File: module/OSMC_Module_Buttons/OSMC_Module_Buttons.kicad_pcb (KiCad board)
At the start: 4 copper layers, 34 x 41 mm, 4 parts, among them J1 Conn_01x08_Socket, U1 OSMC Module Board w/pins, U2 24LC02BT-I/OT, U3 PCF8574DWR

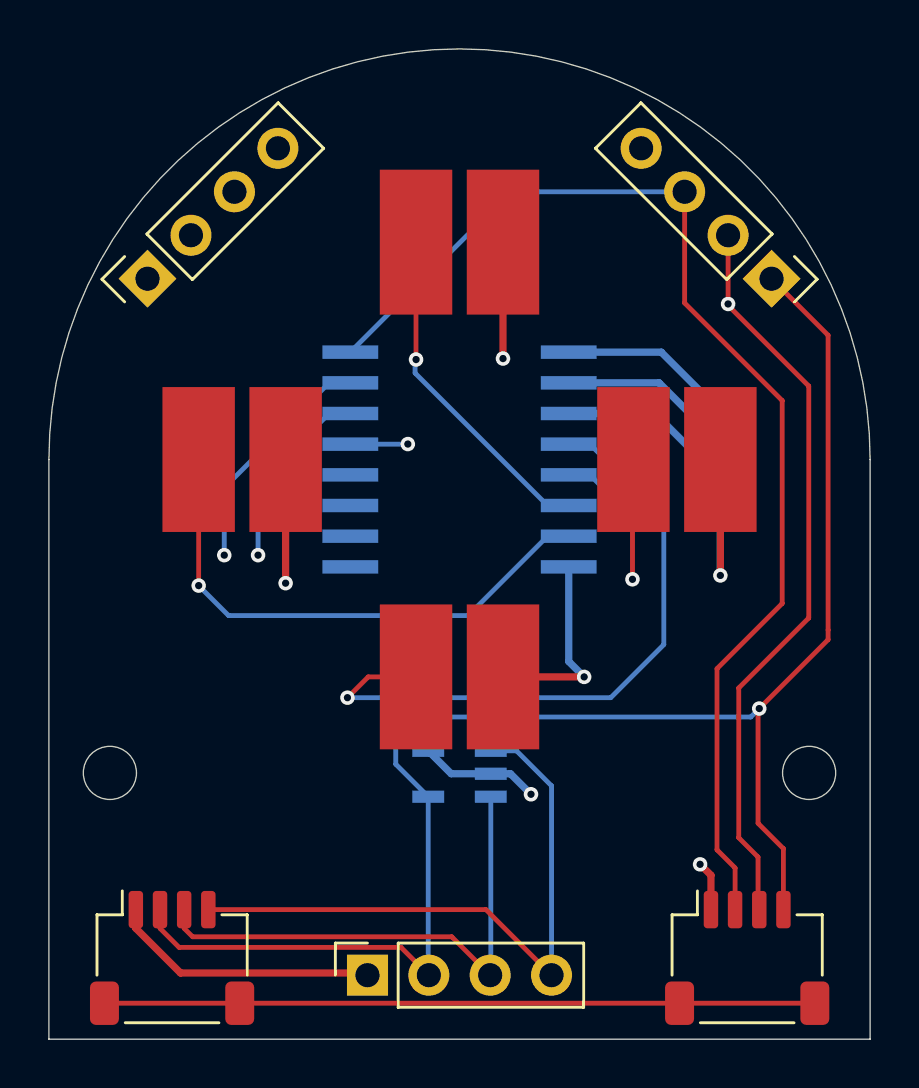
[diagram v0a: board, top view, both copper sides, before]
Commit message: cleared via and traces
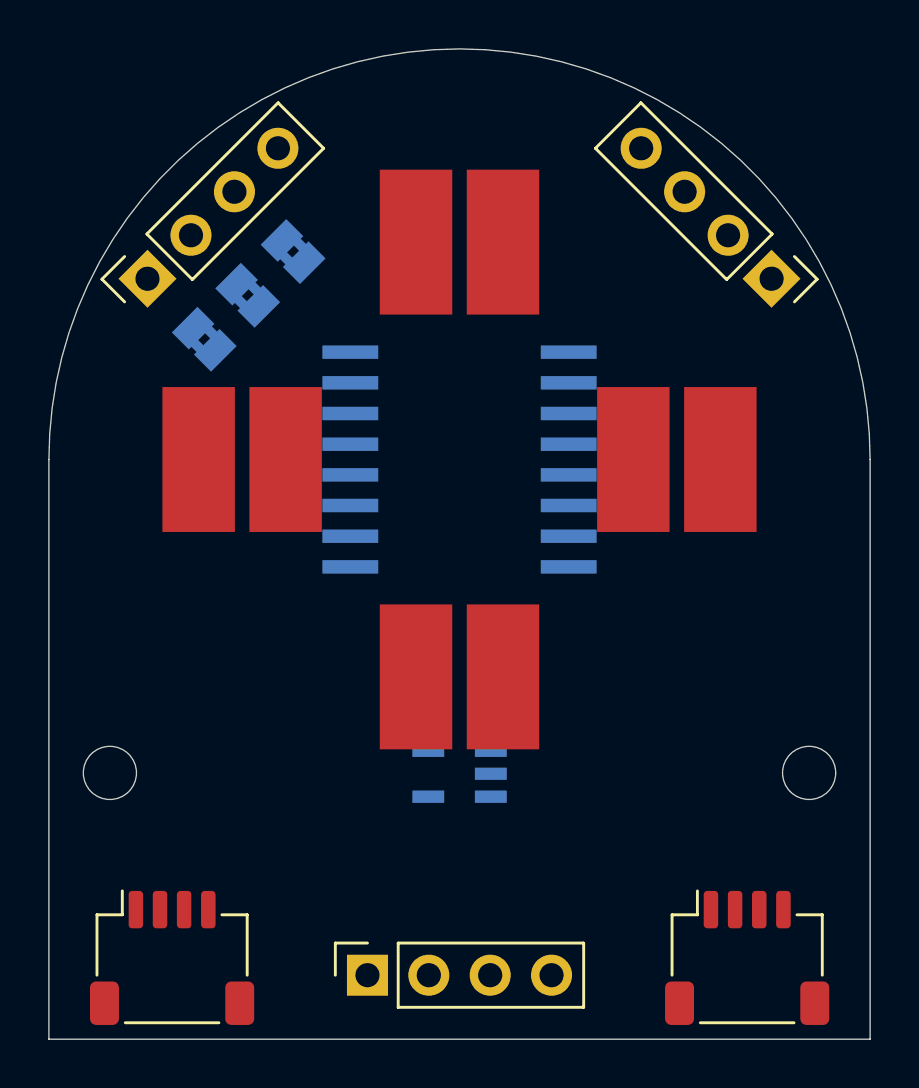
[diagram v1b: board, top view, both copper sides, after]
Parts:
- added JP1: SolderJumper_2_Bridged, Jumper:SolderJumper-2_P1.3mm_Bridged2Bar_Pad1.0x1.5mm, B.Cu at (186.5, 70.8)
- added JP2: SolderJumper_2_Bridged, Jumper:SolderJumper-2_P1.3mm_Bridged2Bar_Pad1.0x1.5mm, B.Cu at (188.3, 68.9)
- added JP3: SolderJumper_2_Bridged, Jumper:SolderJumper-2_P1.3mm_Bridged2Bar_Pad1.0x1.5mm, B.Cu at (190.2, 67.1)
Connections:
- U1 pad 18: unconnected-(U1-A3-Pad18) -> /A2
- U1 pad 19: unconnected-(U1-A2-Pad19) -> /A1
- U1 pad 20: unconnected-(U1-A1-Pad20) -> /A0
- U3 pad 1: GND -> /A0
- U3 pad 16: /5V -> /3v3
- U3 pad 2: GND -> /A1
- U3 pad 3: GND -> /A2
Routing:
- net GND: track 70.8 -> 0.00 mm, vias 6 -> 0
- net /3v3: track 67.4 -> 0.00 mm, vias 1 -> 0
- net /SCL: track 57.4 -> 0.00 mm, vias 1 -> 0
- net /SDA: track 53.4 -> 0.00 mm, vias 1 -> 0
- net /5V: track 49.4 -> 0.00 mm
- net /INT: track 48.8 -> 0.00 mm, vias 2 -> 0
- net unconnected-(U1-PadMP)_3: track 29.4 -> 0.00 mm
- net /B1: track 27.6 -> 0.00 mm, vias 1 -> 0
- net /B4: track 22.4 -> 0.00 mm, vias 1 -> 0
- net /B3: track 14.1 -> 0.00 mm, vias 1 -> 0
- net /B2: track 10.9 -> 0.00 mm, vias 1 -> 0
- added copper zone on In2.Cu, net /3v3

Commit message: modules completed
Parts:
- renumbered JP1 to J1, JP2 to J2, JP3 to J3
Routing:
- net /INT: track 0.00 -> 50.1 mm, vias 0 -> 4
- net /SCL: track 0.00 -> 44.1 mm
- net /SDA: track 0.00 -> 44.1 mm, vias 0 -> 2
- net /5V: track 0.00 -> 30.6 mm, vias 0 -> 1
- net GND: track 0.00 -> 29.3 mm, vias 0 -> 10
- net /A0: track 0.00 -> 25.1 mm, vias 0 -> 1
- net /A1: track 0.00 -> 22.0 mm, vias 0 -> 1
- net /A2: track 0.00 -> 20.5 mm, vias 0 -> 1
- net /B4: track 0.00 -> 20.1 mm, vias 0 -> 1
- net /B1: track 0.00 -> 14.8 mm, vias 0 -> 1
- net /B3: track 0.00 -> 14.6 mm, vias 0 -> 1
- net /3v3: track 0.00 -> 7.54 mm, vias 0 -> 4
- net /B2: track 0.00 -> 2.94 mm, vias 0 -> 1

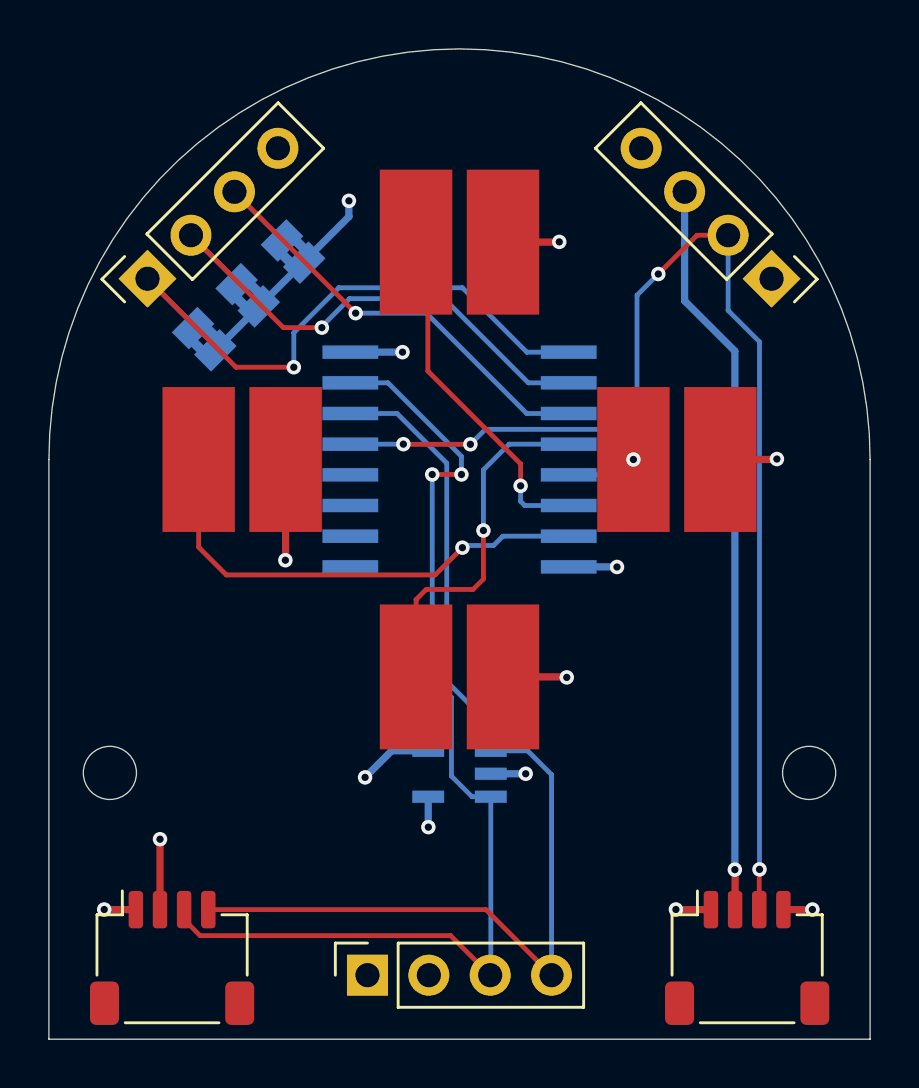
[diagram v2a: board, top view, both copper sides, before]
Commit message: update to modules gerbers produced
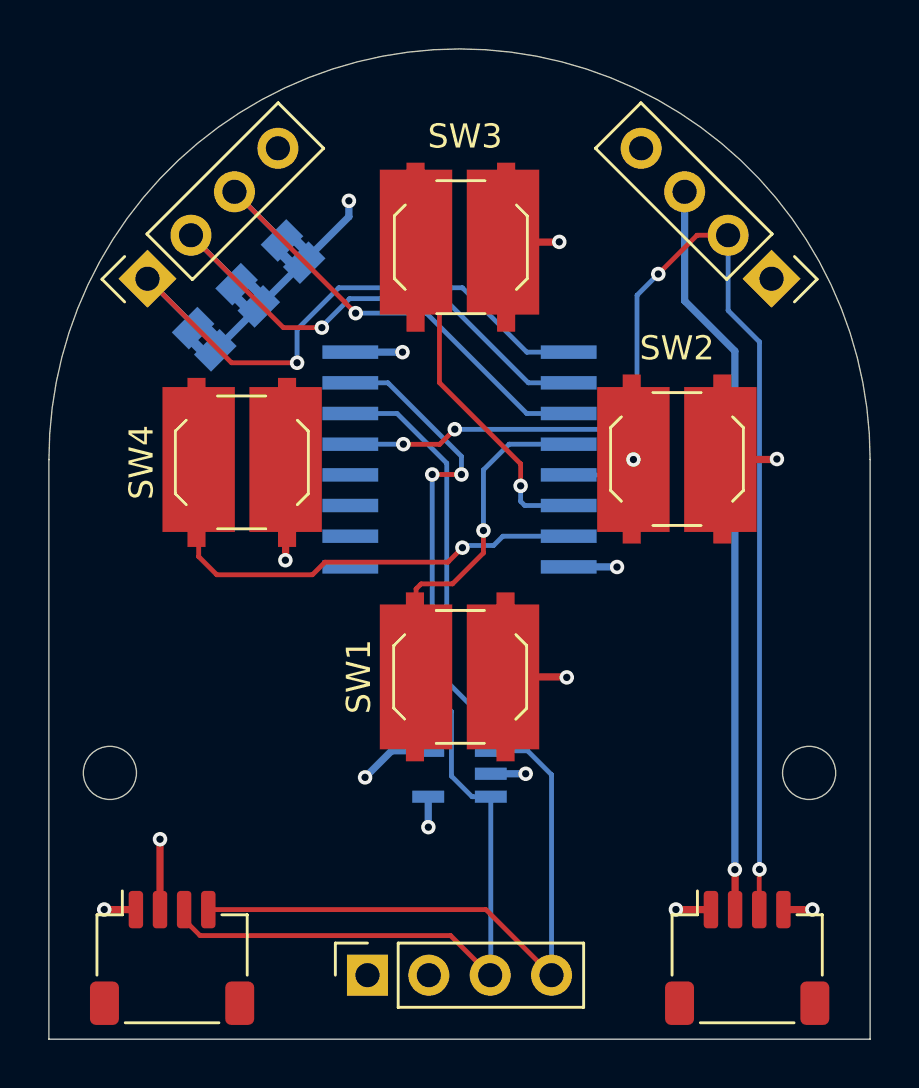
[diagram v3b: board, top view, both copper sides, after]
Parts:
- added SW1: SW_Push, footprints:SW_Push_1P1T_XKB_TS-1187A, F.Cu at (197.1, 84.7)
- added SW2: SW_Push, footprints:SW_Push_1P1T_XKB_TS-1187A, F.Cu at (206.0, 75.7)
- added SW3: SW_Push, footprints:SW_Push_1P1T_XKB_TS-1187A, F.Cu at (197.1, 67.0)
- added SW4: SW_Push, footprints:SW_Push_1P1T_XKB_TS-1187A, F.Cu at (188.0, 75.9)

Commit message: created all gerber zips
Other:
- board text added: "B MOD V1.1 2/26"
